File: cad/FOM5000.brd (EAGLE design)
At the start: 80 x 80 mm, 42 parts, among them Q1 DMN2300U-7, U1 MCP7941X, U2 AT30TS75A-SS, U3 MCP3424-E/SL, U4 MCP1824T-ADJE/OT, Y1 32.768KHz

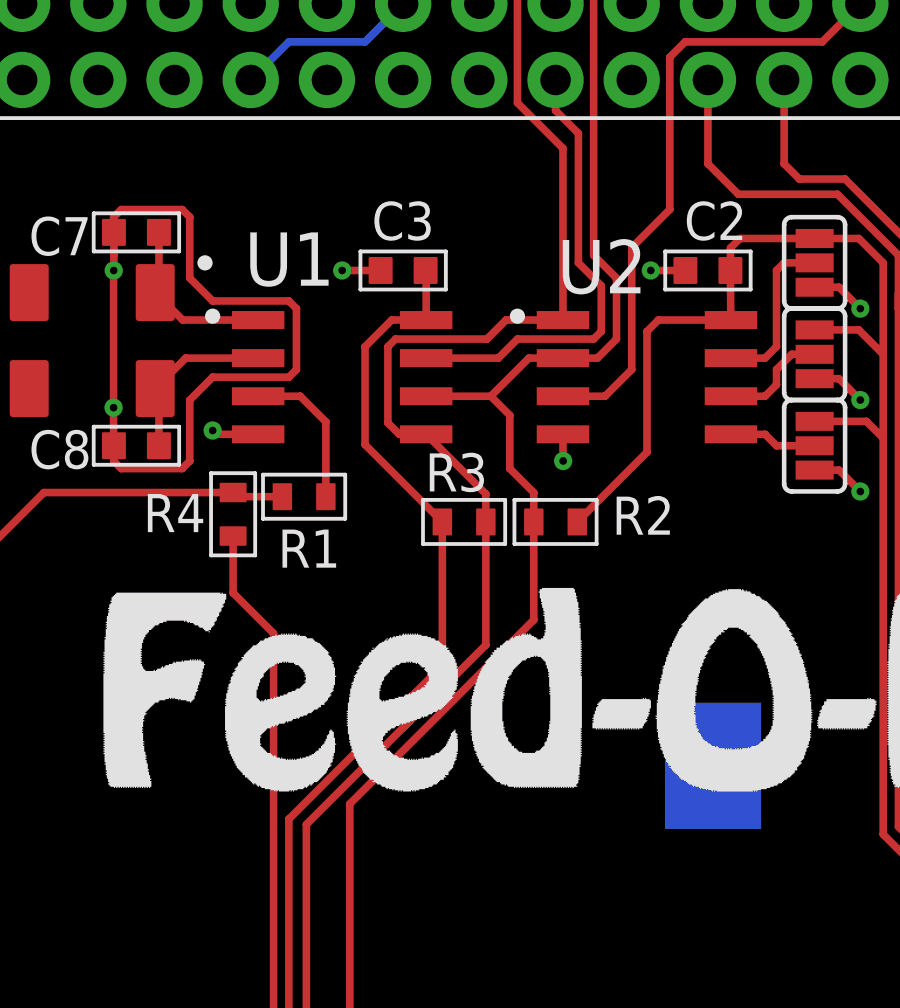
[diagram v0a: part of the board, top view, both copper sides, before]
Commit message: Add pullup resistor on RTCMFP
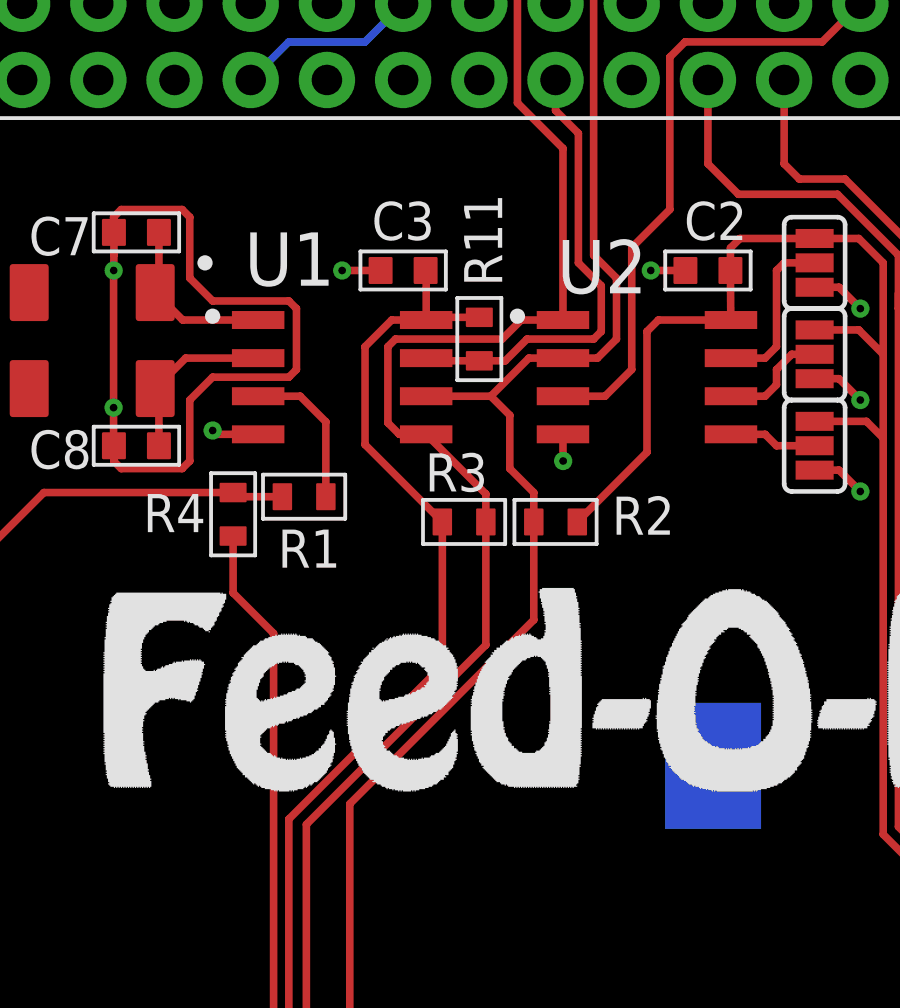
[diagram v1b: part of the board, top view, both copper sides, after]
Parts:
- added R11: 10K 5%, C3-Panasonic:R0603
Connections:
- net RTCMFC: now also R11.1
- net VCC: now also R11.2
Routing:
- net VCC: track 249.6 -> 251.4 mm
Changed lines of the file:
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@@
 <attribute name="VALUE" x="35.941" y="51.308" size="0.4064" layer="27" rot="R270"/>
+</element>
+<element name="R11" library="C3-Panasonic" package="R0603" value="10K 5%" x="26.67" y="53.594" smashed="yes" rot="R90">
+<attribute name="NAME" x="26.162" y="56.896" size="1.27" layer="25" font="vector" ratio="10" rot="R270" align="bottom-center"/>
+<attribute name="VALUE" x="27.94" y="53.594" size="1.27" layer="27" font="vector" rot="R90" align="top-center"/>
 </element>
 </elements>
@@
 <wire x1="32.258" y1="53.848" x2="32.258" y2="49.821" width="0.254" layer="1"/>
 <wire x1="32.258" y1="49.821" x2="29.935" y2="47.498" width="0.254" layer="1"/>
+<contactref element="R11" pad="2"/>
+<wire x1="24.898" y1="54.229" x2="24.988" y2="54.319" width="0.254" layer="1"/>
+<wire x1="24.988" y1="54.319" x2="26.67" y2="54.319" width="0.254" layer="1"/>
 <wire x1="16.51" y1="25.019" x2="16.256" y2="25.019" width="0" layer="19" extent="1-1"/>
 </signal>
@@
 <wire x1="23.622" y1="50.8" x2="23.622" y2="53.34" width="0.254" layer="1"/>
 <wire x1="23.622" y1="53.34" x2="23.876" y2="53.594" width="0.254" layer="1"/>
-<wire x1="23.876" y1="53.594" x2="26.924" y2="53.594" width="0.254" layer="1"/>
-<wire x1="27.559" y1="54.229" x2="29.458" y2="54.229" width="0.254" layer="1"/>
-<wire x1="26.924" y1="53.594" x2="27.559" y2="54.229" width="0.254" layer="1"/>
 <wire x1="29.458" y1="54.229" x2="29.458" y2="59.95" width="0.254" layer="1"/>
 <wire x1="29.458" y1="59.95" x2="27.94" y2="61.468" width="0.254" layer="1"/>
 <wire x1="20.9042" y1="25.654" x2="20.9042" y2="37.4142" width="0.254" layer="1"/>
-<wire x1="20.9042" y1="37.4142" x2="24.13" y2="40.64" width="0.254" layer="1"/>
-<wire x1="24.13" y1="40.64" x2="24.347" y2="40.857" width="0.254" layer="1"/>
-<wire x1="24.13" y1="40.64" x2="26.887" y2="43.397" width="0.254" layer="1"/>
+<wire x1="20.9042" y1="37.4142" x2="26.887" y2="43.397" width="0.254" layer="1"/>
 <wire x1="26.887" y1="43.397" x2="26.887" y2="47.498" width="0.254" layer="1"/>
 <wire x1="26.887" y1="47.498" x2="26.887" y2="48.43" width="0.254" layer="1"/>
 <wire x1="26.887" y1="48.43" x2="24.898" y2="50.419" width="0.254" layer="1"/>
+<wire x1="28.067" y1="54.229" x2="29.458" y2="54.229" width="0.254" layer="1"/>
+<wire x1="27.432" y1="53.594" x2="28.067" y2="54.229" width="0.254" layer="1"/>
+<wire x1="23.876" y1="53.594" x2="27.432" y2="53.594" width="0.254" layer="1"/>
 <wire x1="31.75" y1="67.056" x2="31.496" y2="67.056" width="0" layer="19" extent="1-1"/>
 </signal>
@@
 <signal name="RTCMFC">
 <contactref element="U1" pad="7"/>
-<wire x1="24.898" y1="52.959" x2="27.305" y2="52.959" width="0.254" layer="1"/>
-<wire x1="27.305" y1="52.959" x2="27.94" y2="53.594" width="0.254" layer="1"/>
-<wire x1="27.94" y1="53.594" x2="30.48" y2="53.594" width="0.254" layer="1"/>
 <wire x1="30.48" y1="53.594" x2="30.734" y2="53.848" width="0.254" layer="1"/>
 <wire x1="30.734" y1="53.848" x2="30.734" y2="55.372" width="0.254" layer="1"/>
@@
 <wire x1="29.21" y1="61.214" x2="29.21" y2="62.23" width="0.254" layer="1"/>
 <wire x1="29.972" y1="60.452" x2="29.21" y2="61.214" width="0.254" layer="1"/>
+<contactref element="R11" pad="1"/>
+<wire x1="24.898" y1="52.959" x2="24.988" y2="52.869" width="0.254" layer="1"/>
+<wire x1="24.988" y1="52.869" x2="26.67" y2="52.869" width="0.254" layer="1"/>
+<wire x1="26.67" y1="52.869" x2="27.5357375" y2="52.869" width="0.254" layer="1"/>
+<wire x1="28.2607375" y1="53.594" x2="30.48" y2="53.594" width="0.254" layer="1"/>
+<wire x1="27.5357375" y1="52.869" x2="28.2607375" y2="53.594" width="0.254" layer="1"/>
 </signal>
 <signal name="N$1">

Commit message: Rename mislabeled net RTCMFP
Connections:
- net RTCMFC renamed RTCMFP
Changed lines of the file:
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@@
 <wire x1="36.576" y1="50.038" x2="37.846" y2="50.038" width="0.254" layer="1"/>
 </signal>
-<signal name="RTCMFC">
+<signal name="RTCMFP">
 <contactref element="U1" pad="7"/>
 <wire x1="30.48" y1="53.594" x2="30.734" y2="53.848" width="0.254" layer="1"/>

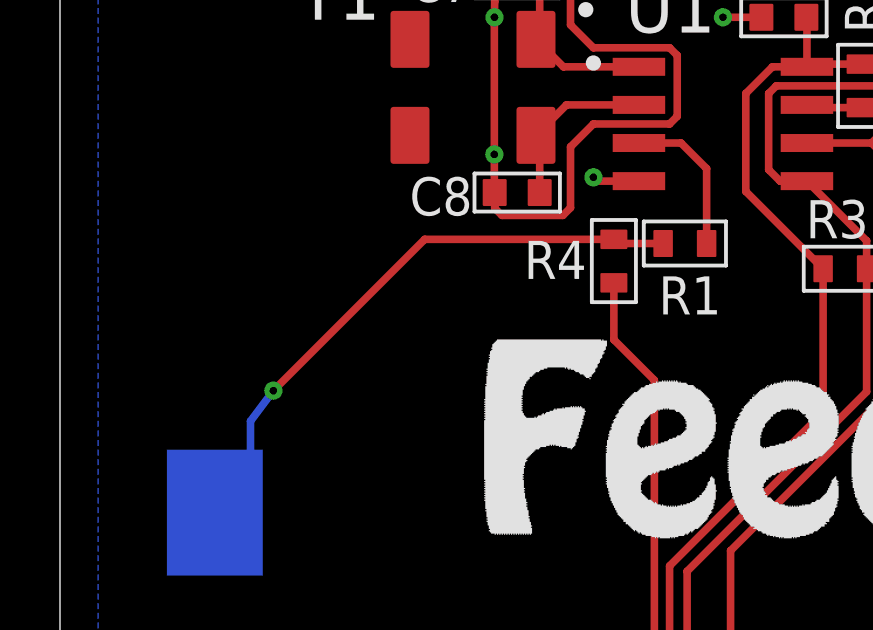
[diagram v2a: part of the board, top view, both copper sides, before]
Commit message: Add schottky diode on VBAT for UL compliance; change VBAT load limiting resistor to 1K per AN-1365
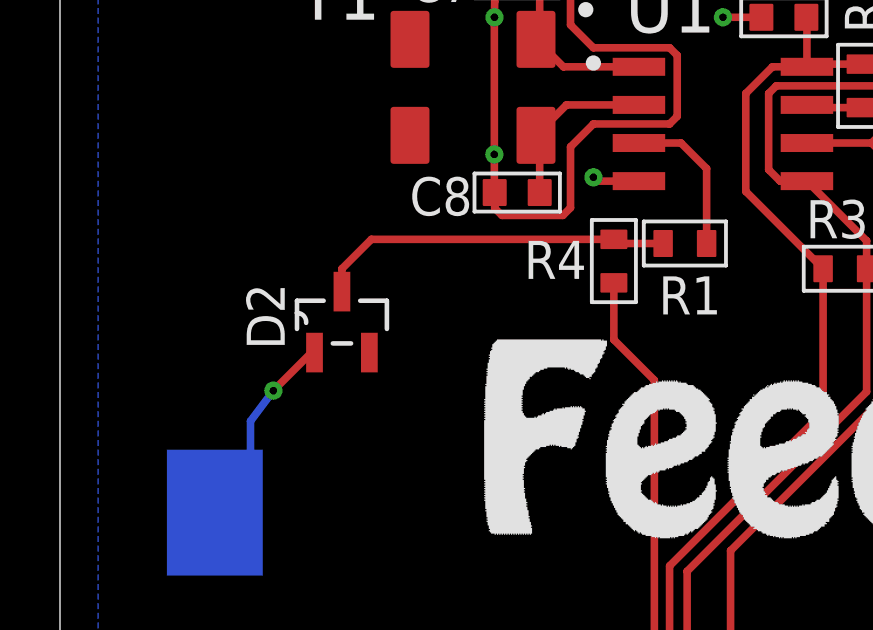
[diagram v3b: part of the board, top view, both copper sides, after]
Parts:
- added D2: BAT54, C3-RCL:SOT23-3
- R1: value 100R 5% -> 1K 5%
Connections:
- new net N$2: D2.C, R1.1, R4.1
- net VBAT: now also D2.A; no longer R1.1, R4.1
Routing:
- net VBAT: track 21.3 -> 8.03 mm
- net N$2: track 0.00 -> 11.9 mm
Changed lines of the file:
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@@
 </element>
 <element name="B1" library="C3-Battery" package="BU2032SM-HD" value="CR2032" x="19.812" y="39.37" locked="yes" rot="MR180"/>
-<element name="R1" library="C3-Panasonic" package="R0603" value="100R 5%" x="20.82931875" y="48.33945" smashed="yes">
+<element name="R1" library="C3-Panasonic" package="R0603" value="1K 5%" x="20.82931875" y="48.33945" smashed="yes">
 <attribute name="NAME" x="20.998153125" y="47.244028125" size="1.27" layer="25" font="vector" ratio="10" rot="R180" align="bottom-center"/>
-<attribute name="VALUE" value="100R 5%" x="20.82931875" y="48.33945" size="1.778" layer="27" display="off"/>
+<attribute name="VALUE" value="1K 5%" x="20.82931875" y="48.33945" size="1.778" layer="27" display="off"/>
 <attribute name="VALUE" x="20.82931875" y="47.06945" size="1.27" layer="27" font="vector" align="top-center"/>
 </element>
@@
 <attribute name="VALUE" x="27.94" y="53.594" size="1.27" layer="27" font="vector" rot="R90" align="top-center"/>
 </element>
+<element name="D2" library="C3-RCL" package="SOT23-3" value="BAT54" x="9.398" y="45.72" rot="R90"/>
 </elements>
 <signals>
@@
 <signal name="VBAT">
 <contactref element="B1" pad="P"/>
-<contactref element="R1" pad="1"/>
-<contactref element="R4" pad="1"/>
-<wire x1="20.10431875" y1="48.33945" x2="18.6015" y2="48.33945" width="0.254" layer="1"/>
-<wire x1="18.462553125" y1="48.478396875" x2="18.6015" y2="48.33945" width="0.254" layer="1"/>
 <wire x1="6.096" y1="40.304" x2="5.162" y2="39.37" width="0.254" layer="16"/>
 <wire x1="5.162" y1="39.37" x2="6.35" y2="40.558" width="0.254" layer="16"/>
@@
 <wire x1="6.35" y1="42.418" x2="7.112" y2="43.434" width="0.254" layer="16"/>
 <via x="7.112" y="43.434" extent="1-16" drill="0.254" diameter="0.508"/>
-<wire x1="7.112" y1="43.434" x2="12.156396875" y2="48.478396875" width="0.254" layer="1"/>
-<wire x1="12.156396875" y1="48.478396875" x2="18.462553125" y2="48.478396875" width="0.254" layer="1"/>
+<contactref element="D2" pad="A"/>
+<wire x1="8.4836" y1="44.704" x2="8.382" y2="44.704" width="0.254" layer="1"/>
+<wire x1="8.382" y1="44.704" x2="7.112" y2="43.434" width="0.254" layer="1"/>
 </signal>
 <signal name="VCC">
@@
 </polygon>
 </signal>
+<signal name="N$2">
+<contactref element="R1" pad="1"/>
+<contactref element="R4" pad="1"/>
+<contactref element="D2" pad="C"/>
+<wire x1="20.10431875" y1="48.33945" x2="18.6015" y2="48.33945" width="0.254" layer="1"/>
+<wire x1="18.462553125" y1="48.478396875" x2="18.6015" y2="48.33945" width="0.254" layer="1"/>
+<wire x1="9.398" y1="46.736" x2="9.398" y2="47.498" width="0.254" layer="1"/>
+<wire x1="10.378396875" y1="48.478396875" x2="18.462553125" y2="48.478396875" width="0.254" layer="1"/>
+<wire x1="9.398" y1="47.498" x2="10.378396875" y2="48.478396875" width="0.254" layer="1"/>
+</signal>
 </signals>
+<errors>
+</errors>
 </board>
 </drawing>

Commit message: Added some input capacitance
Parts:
- added C11: 100uF, C3-Nichicon:8MM_SMD
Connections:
- net 5V: now also C11.P
- net GND: now also C11.N
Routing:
- net GND: track 71.4 -> 74.6 mm, vias 19 -> 20
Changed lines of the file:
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@@
 </element>
 <element name="D2" library="C3-RCL" package="SOT23-3" value="BAT54" x="9.398" y="45.72" rot="R90"/>
+<element name="C11" library="C3-Nichicon" package="8MM_SMD" value="100uF" x="70.104" y="29.718" smashed="yes">
+<attribute name="HEIGHT" value="10mm" x="70.104" y="29.718" size="1.778" layer="27" display="off"/>
+<attribute name="NAME" x="72.111" y="34.235" size="1.778" layer="25" font="vector" ratio="10" align="bottom-center"/>
+<attribute name="VALUE" x="70.179" y="24.693" size="1.27" layer="27" font="vector" align="top-center"/>
+</element>
 </elements>
 <signals>
@@
 <wire x1="57.15" y1="64.77" x2="58.42" y2="63.5" width="0.254" layer="1"/>
 <wire x1="58.42" y1="63.5" x2="58.42" y2="53.34" width="0.254" layer="1"/>
-<wire x1="68.109" y1="37.846" x2="68.109" y2="36.031" width="0.254" layer="1"/>
-<wire x1="68.109" y1="36.031" x2="72.39" y2="30.48" width="0.254" layer="1"/>
-<wire x1="72.39" y1="30.48" x2="72.39" y2="12.7" width="0.254" layer="1"/>
 <wire x1="72.39" y1="12.7" x2="71.12" y2="11.43" width="0.254" layer="1"/>
 <wire x1="71.12" y1="11.43" x2="64.77" y2="11.43" width="0.254" layer="1"/>
@@
 <wire x1="24.898" y1="54.229" x2="24.988" y2="54.319" width="0.254" layer="1"/>
 <wire x1="24.988" y1="54.319" x2="26.67" y2="54.319" width="0.254" layer="1"/>
+<wire x1="68.109" y1="34.761" x2="69.85" y2="33.02" width="0.254" layer="1"/>
+<wire x1="69.85" y1="33.02" x2="69.85" y2="24.13" width="0.254" layer="1"/>
+<wire x1="69.85" y1="24.13" x2="72.39" y2="21.59" width="0.254" layer="1"/>
+<wire x1="72.39" y1="21.59" x2="72.39" y2="12.7" width="0.254" layer="1"/>
+<wire x1="68.109" y1="37.846" x2="68.109" y2="34.761" width="0.254" layer="1"/>
 <wire x1="16.51" y1="25.019" x2="16.256" y2="25.019" width="0" layer="19" extent="1-1"/>
 </signal>
@@
 <wire x1="49.53" y1="17.654" x2="48.386" y2="17.654" width="0.254" layer="1"/>
 <wire x1="48.386" y1="17.654" x2="48.006" y2="18.034" width="0.254" layer="1"/>
+<contactref element="C11" pad="N"/>
+<wire x1="73.154" y1="29.718" x2="73.154" y2="29.716" width="0.254" layer="1"/>
+<wire x1="73.154" y1="29.716" x2="75.438" y2="27.432" width="0.254" layer="1"/>
+<via x="75.438" y="27.432" extent="1-16" drill="0.254" diameter="0.508"/>
 </signal>
 <signal name="VBAT_IN">
@@
 <wire x1="57.912" y1="60.96" x2="56.642" y2="62.23" width="0.254" layer="1"/>
 <wire x1="56.642" y1="62.23" x2="54.61" y2="62.23" width="0.254" layer="1"/>
-<wire x1="66.802" y1="26.416" x2="66.802" y2="44.196" width="0.254" layer="1"/>
-<wire x1="66.802" y1="44.196" x2="57.912" y2="53.086" width="0.254" layer="1"/>
+<wire x1="57.912" y1="53.086" x2="66.802" y2="44.196" width="0.254" layer="1"/>
 <wire x1="57.912" y1="53.086" x2="57.912" y2="60.96" width="0.254" layer="1"/>
+<contactref element="C11" pad="P"/>
+<wire x1="66.802" y1="26.416" x2="66.802" y2="29.466" width="0.254" layer="1"/>
+<wire x1="67.054" y1="29.718" x2="66.802" y2="29.466" width="0.254" layer="1"/>
+<wire x1="66.802" y1="44.196" x2="66.802" y2="29.97" width="0.254" layer="1"/>
+<wire x1="66.802" y1="29.97" x2="67.054" y2="29.718" width="0.254" layer="1"/>
 </signal>
 <signal name="BSENSE">

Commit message: Change R9 to 330R
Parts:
- LED1: value RED Bulk 5mm -> 1.9Vf, 25mA
- R9: value 100R 5% -> 330R 5%
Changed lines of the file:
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@@
 <attribute name="VALUE" x="49.276" y="21.59" size="1.27" layer="27" font="vector" align="top-center"/>
 </element>
-<element name="LED1" library="C3-LED" package="LED5MM" value="RED Bulk 5mm" x="67" y="40" locked="yes" smashed="yes" rot="MR0">
+<element name="LED1" library="C3-LED" package="LED5MM" value="1.9Vf, 25mA" x="67" y="40" locked="yes" smashed="yes" rot="MR0">
 <attribute name="NAME" x="63.825" y="40.5334" size="1.27" layer="26" ratio="10" rot="MR0"/>
 <attribute name="VALUE" x="63.7996" y="38.1966" size="1.27" layer="28" ratio="10" rot="MR0"/>
 </element>
-<element name="R9" library="C3-Panasonic" package="R0603" value="100R 5%" x="68.834" y="37.846" smashed="yes" rot="R180">
+<element name="R9" library="C3-Panasonic" package="R0603" value="330R 5%" x="68.834" y="37.846" smashed="yes" rot="R180">
 <attribute name="NAME" x="66.04" y="37.338" size="1.27" layer="25" font="vector" ratio="10" align="bottom-center"/>
-<attribute name="VALUE" x="68.834" y="39.116" size="1.27" layer="27" font="vector" rot="R180" align="top-center"/>
+<attribute name="VALUE" value="330R 5%" x="68.834" y="39.116" size="1.27" layer="27" font="vector" rot="R180" align="top-center"/>
 </element>
 <element name="UART" library="C3-Connector" package="100-1X04-TH-040" value="UART" x="44.45" y="55.118" smashed="yes">
